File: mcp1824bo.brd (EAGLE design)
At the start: 53.3 x 12.1 mm, 20 parts, among them J1 M02PTH, J2 M02PTH, J3 M02PTH, J4 10118194-0001LF, U4 MCP1824T-ADJE/OT

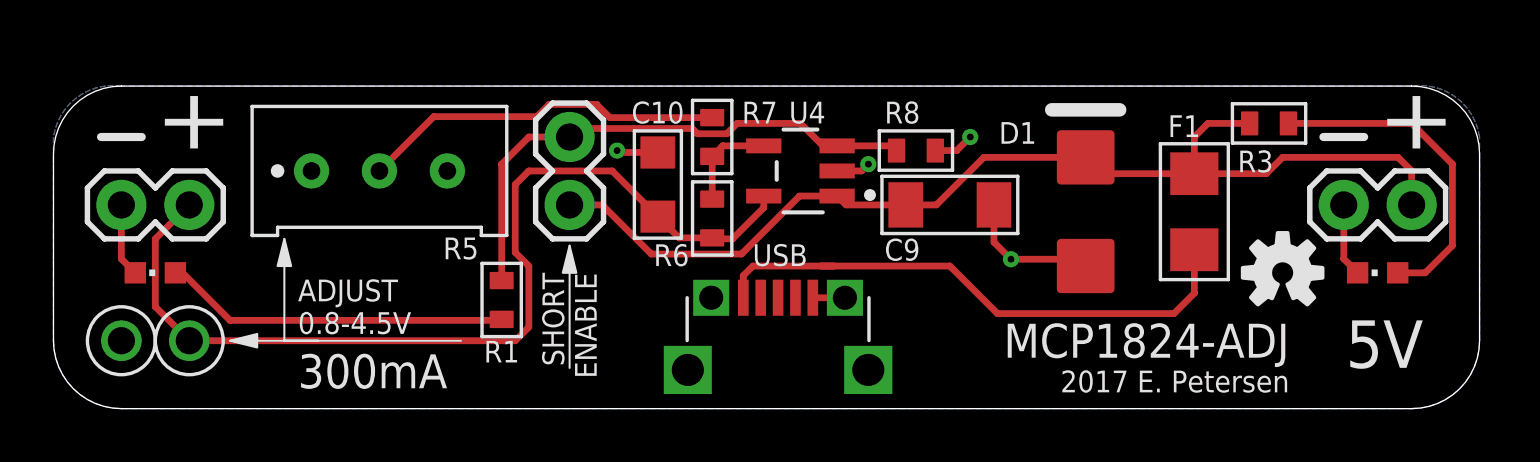
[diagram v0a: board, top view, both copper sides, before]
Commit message: replace SHDN jumper with a slide switch
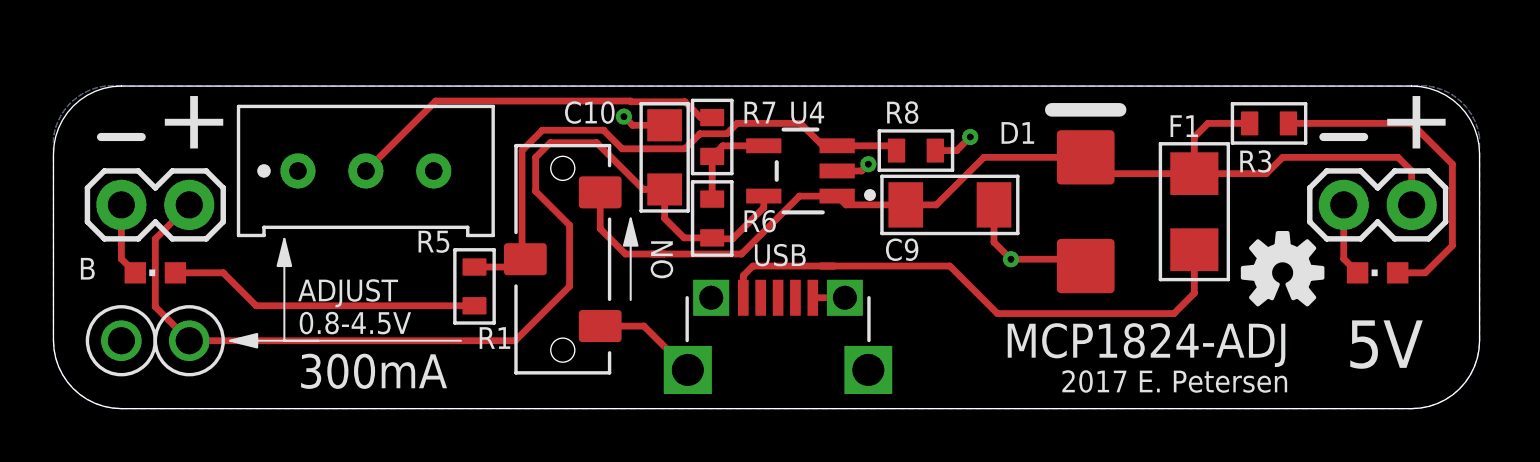
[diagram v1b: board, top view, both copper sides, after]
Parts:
- removed J3: M02PTH, C3-Connector:1X02
- added SW1: CL-SB-12A-01, C3-Switches:CL-SB-12A
- moved R1 1.14 mm to (15.7, 4.57)
- moved C10 1.05 mm to (22.9, 9.40)
- moved R5 0.51 mm to (11.7, 8.89)
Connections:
- net GND: now also SW1.1
- net SHDN: now also SW1.C; no longer J3.2
- net VIN: now also SW1.3; no longer J3.1
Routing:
- net GND: track 16.2 -> 20.3 mm
- net VOUT: track 36.1 -> 38.4 mm
- net SHDN: track 20.3 -> 21.6 mm
- net LED1: track 13.0 -> 12.0 mm
- net ADJ2: track 13.7 -> 14.3 mm
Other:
- board text added: ">COPY"
- board text added: ">REV"
- board text added: ">TITLE"
- board text added: "ON"
- board text removed: "2017 E. Petersen"
- board text removed: "MCP1824-ADJ"
- board text removed: "SHORT ENABLE"
